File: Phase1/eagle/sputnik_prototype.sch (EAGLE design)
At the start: 6 parts, among them U1 MEGA128-M

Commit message: Added stuff to RF schematic
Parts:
- added C1, C10, C11, C12, C13, C14, C2, C3, C4, C5, C6, C7, C8, C9: (no value), rcl_custom:C-EU0603-B-NOSILK
- added L1, L2, L3, L4, L5, L6: (no value), rcl_custom:L-US0603-B-NOSILK
- added U$2: SMAJ716-ND, psas_c3_team05:SMAJ716-ND
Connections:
- new net N$10: C5.2, C7.1, L3.1
- new net N$16: C7.2, C9.2, L3.2, L5.1
- new net N$17: C11.2, C14.2, L5.2
- new net N$18: C6.2, C8.1, L4.1
- new net N$19: C10.2, C8.2, L4.2, L6.1
- new net N$20: C12.2, C13.2, L6.2
- new net N$6: C4.1, C6.1, L2.2, U$1.RFIO
- new net N$7: C2.1, C5.1, L1.2, U$1.PA_BOOST
- new net N$8: C1.2, C3.1, L1.1, L2.1, U$1.VR_PA
- new net N$9: C13.1, C14.1, U$2.CENTERCONDUCTOR
- net GND: now also C1.1, C10.1, C11.1, C12.1, C2.2, C3.2, C4.2, C9.1, U$2.OUTERCONDUCTOR

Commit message: RF schematic update. Finished PA footprint
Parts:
- added U$3: SKY65116, psas_c3_team05:SKY65116
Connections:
- net GND: now also U1.GND@2; no longer U1.GND1
- net V+: now also U1.VCC@1; no longer U1.VCC1
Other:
- note added: "William Harrington, James Heath"
- note removed: "William Harrington"
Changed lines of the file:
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@@
 <part name="U$2" library="psas_c3_team05" deviceset="SMAJ716-ND" device=""/>
 <part name="GND13" library="psas_c3_team05" deviceset="GND" device=""/>
+<part name="U$3" library="psas_c3_team05" deviceset="SKY65116" device=""/>
 </parts>
 <sheets>
 <sheet>
 <plain>
-<text x="327.66" y="30.48" size="2.54" layer="97">William Harrington</text>
+<text x="327.66" y="30.48" size="2.54" layer="97">William Harrington, James Heath</text>
 <wire x1="10.16" y1="254" x2="63.5" y2="254" width="0.1524" layer="97" style="longdash"/>
 <wire x1="63.5" y1="254" x2="63.5" y2="167.64" width="0.1524" layer="97" style="longdash"/>
@@
 <instance part="U$2" gate="G$1" x="515.62" y="345.44" rot="MR0"/>
 <instance part="GND13" gate="1" x="515.62" y="330.2"/>
+<instance part="U$3" gate="G$1" x="510.54" y="378.46"/>
 </instances>
 <busses>
@@
 <wire x1="86.36" y1="66.04" x2="68.58" y2="66.04" width="0.1524" layer="91"/>
 <junction x="68.58" y="66.04"/>
-<pinref part="U1" gate="G$1" pin="GND1"/>
+<pinref part="U1" gate="G$1" pin="GND@2"/>
 <wire x1="144.78" y1="132.08" x2="68.58" y2="132.08" width="0.1524" layer="91"/>
 <junction x="68.58" y="132.08"/>
@@
 <wire x1="144.78" y1="147.32" x2="96.52" y2="147.32" width="0.1524" layer="91"/>
 <junction x="96.52" y="147.32"/>
-<pinref part="U1" gate="G$1" pin="VCC1"/>
+<pinref part="U1" gate="G$1" pin="VCC@1"/>
 <wire x1="144.78" y1="139.7" x2="96.52" y2="139.7" width="0.1524" layer="91"/>
 <junction x="96.52" y="139.7"/>

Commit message: Added more RF schematic and made LNA footprint
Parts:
- added C15, C16, C17, C18, C19, C20, C21, C22, C23, C24, C25, C26, C27: (no value), rcl_custom:C-EU0603-B-NOSILK
- added L7, L8, L9: (no value), rcl_custom:L-US0603-B-NOSILK
- added R1: (no value), rcl_custom:R-US_0603-B-NOSILK
- added U$4: MAAL-010704, sputnik:MAAL-010704
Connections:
- new net N$21: C14.1, U$3.RFIN
- new net N$22: U$3.RFOUT
- new net N$23: C13.1
- new net N$24: L7.1, U$4.RFIN
- new net N$25: C23.2, L7.2
- new net N$26: C23.1
- new net N$27: R1.1, U$4.VBIAS
- new net N$28: U$1.RXTX
- new net N$29: U$2.CENTERCONDUCTOR
- new net N$31: L9.1
- new net N$32: C26.1, C27.1, L9.2
- net GND: now also C15.1, C16.1, C17.1, C18.1, C19.1, C20.1, C21.1, C22.1, C24.2, C25.2, C26.2, C27.2, U$3.GND, U$3.GND1, U$3.GND2, U$3.GND3, U$3.GND4, U$3.GND5, U$4.GND, U$4.GND2, U$4.NC
- net N$9: now also L8.1, U$4.RFOUT; no longer C13.1, C14.1, U$2.CENTERCONDUCTOR
- net V+: now also C15.2, C16.2, C17.2, C18.2, C19.2, C20.2, C21.2, C22.2, C24.1, C25.1, L8.2, R1.2, U$3.VCC1, U$3.VCC2, U$3.VCNT, U$3.VREF
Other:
- note added: "Switch goes here"
- moved on the sheet: C1, C10, C11, C12, C13, C14, C2, C3, C4, C5, C6, C7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

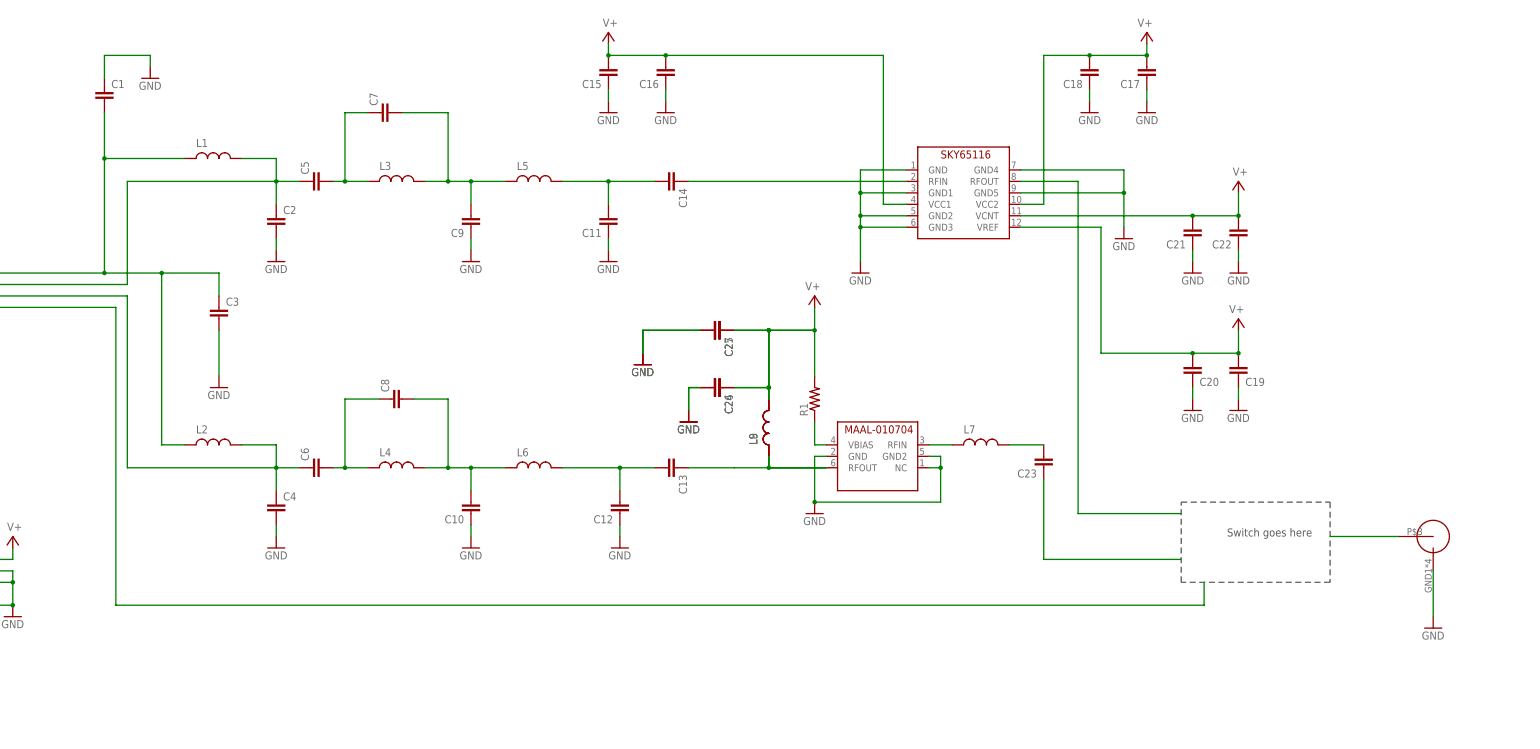
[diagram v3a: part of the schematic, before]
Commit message: Finished 1st draft RF schematic and RF switch footprint
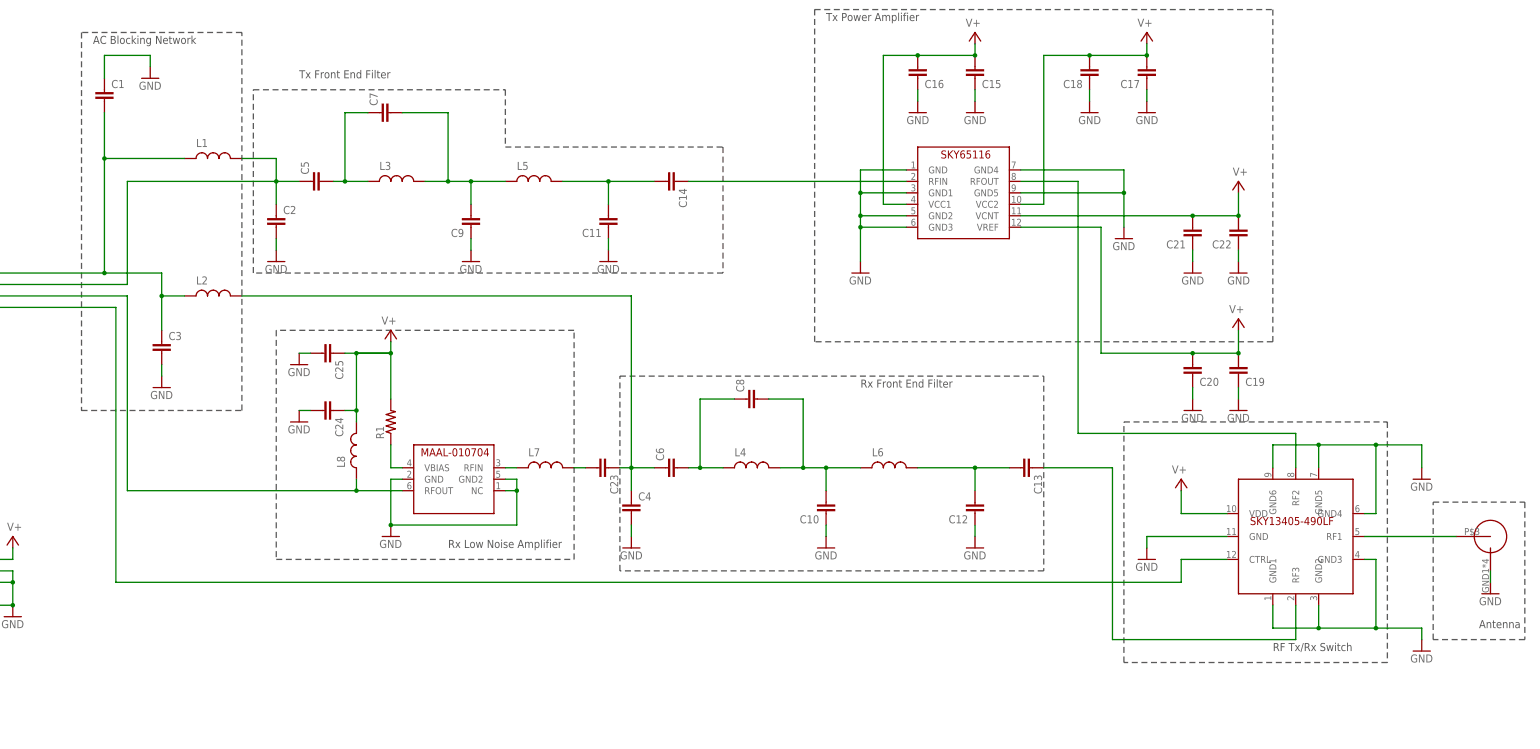
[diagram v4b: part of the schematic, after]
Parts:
- removed C26, C27: (no value), rcl_custom:C-EU0603-B-NOSILK
- removed L9: (no value), rcl_custom:L-US0603-B-NOSILK
- added U$5: SKY13405-490LF, psas_c3_team05:SKY13405-490LF
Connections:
- removed net N$23: C13.1
- removed net N$29 (its old number): U$2.CENTERCONDUCTOR
- removed net N$31: L9.1
- removed net N$32: C26.1, C27.1, L9.2
- removed net N$6: C4.1, C6.1, L2.2, U$1.RFIO
- new net N$30: U$2.CENTERCONDUCTOR, U$5.RF1
- new net N$33: C23.1, C4.1, C6.1, L2.2
- net GND: now also U$5.GND, U$5.GND1, U$5.GND2, U$5.GND3, U$5.GND4, U$5.GND5, U$5.GND6; no longer C26.2, C27.2
- net N$22: now also U$5.RF2
- net N$26: now also C13.1, U$5.RF3; no longer C23.1
- net N$28: now also U$5.CTRL
- net N$9: now also U$1.RFIO
- net V+: now also U$5.VDD
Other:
- note added: "AC Blocking Network"
- note added: "Antenna"
- note added: "RF Tx/Rx Switch"
- note added: "Rx Front End Filter"
- note added: "Rx Low Noise Amplifier"
- note added: "Tx Front End Filter"
- note added: "Tx Power Amplifier"
- note removed: "Switch goes here"
- moved on the sheet: C10, C12, C13, C15, C16, C23, C24, C25, C3, C4, C6, C8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

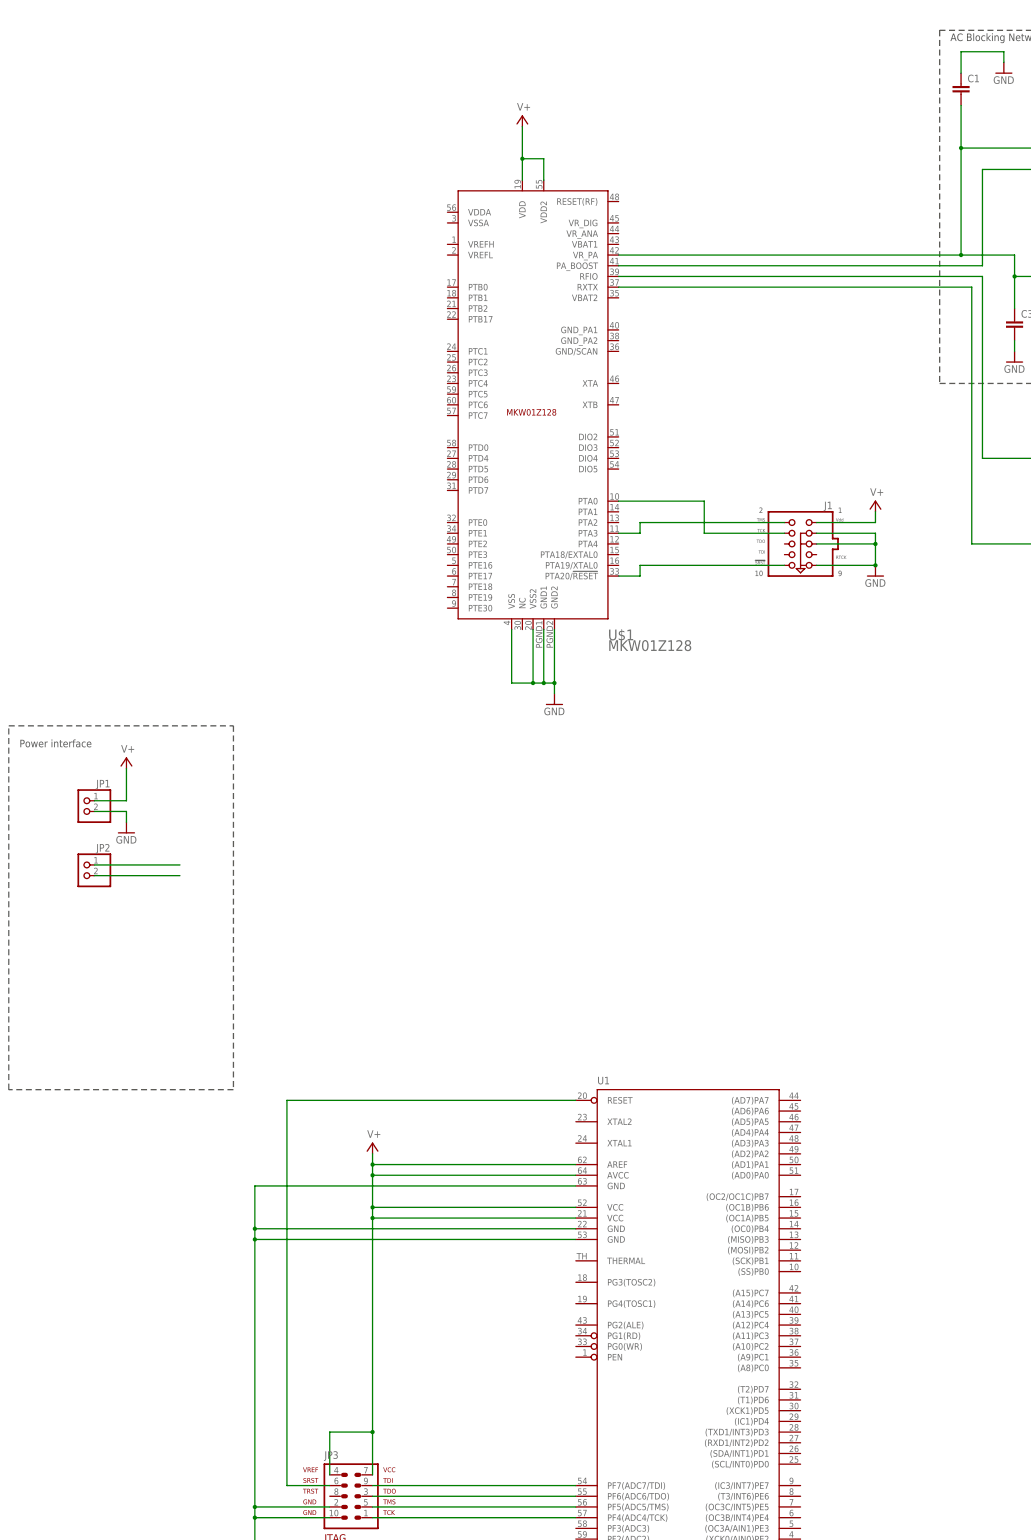
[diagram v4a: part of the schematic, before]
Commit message: Schematic checkpoint
Setup GPIO and I2C for power interface. Placed bypass caps on all power lines. Placed XTAL/Resonator. Labeled some wires.
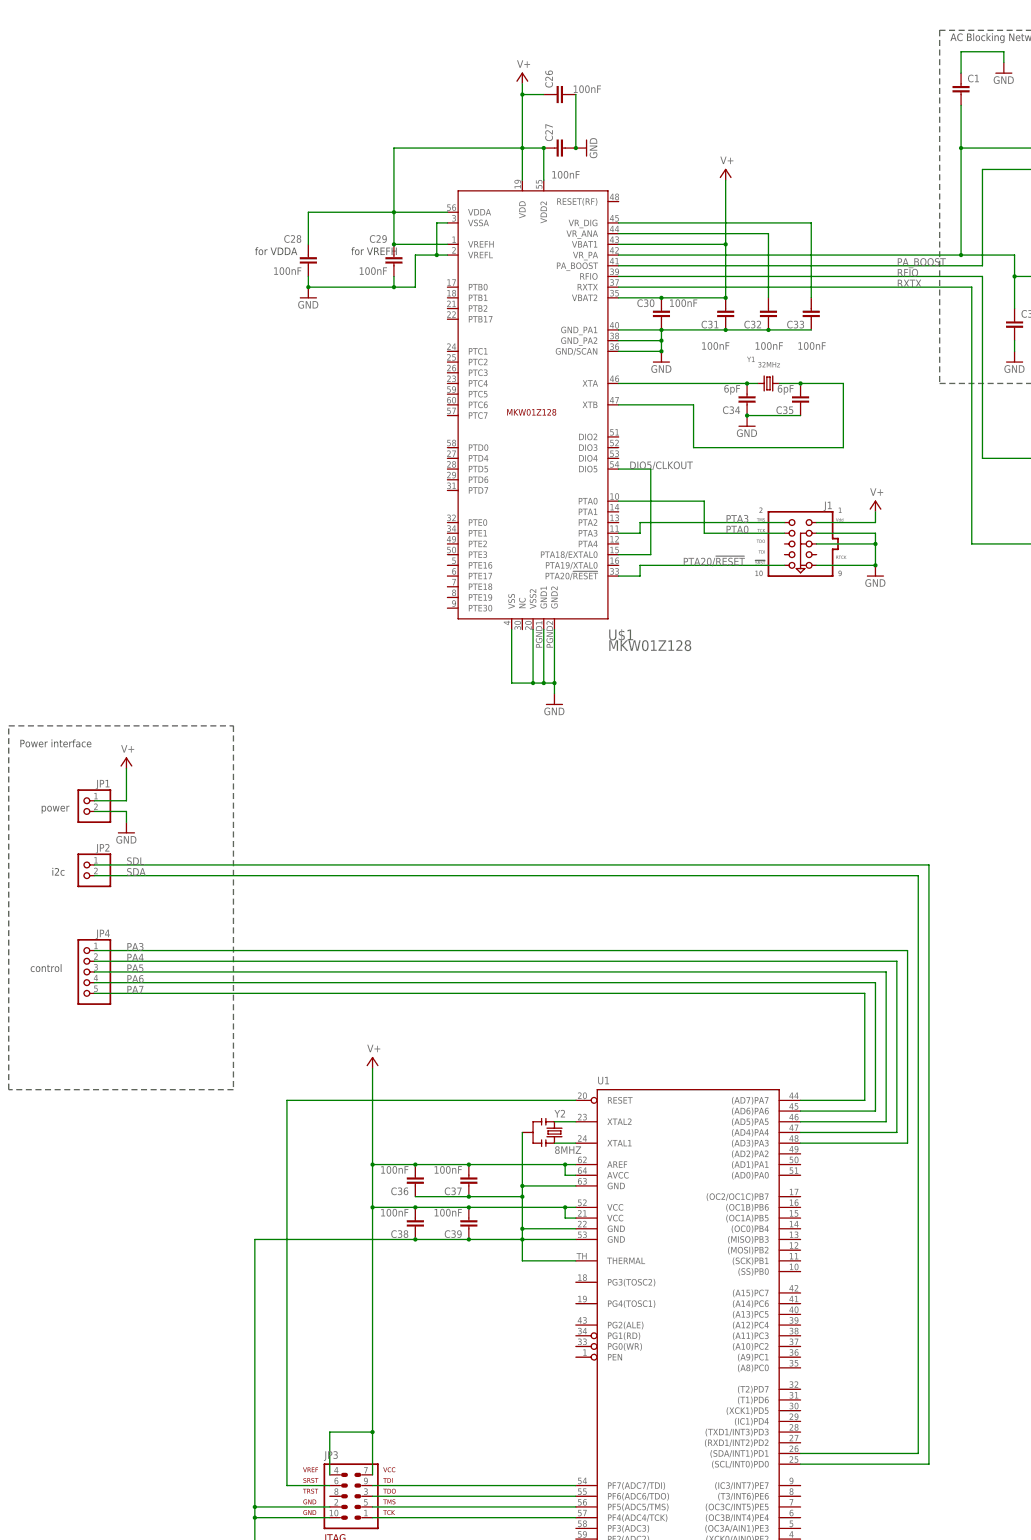
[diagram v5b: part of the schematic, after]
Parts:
- added C26, C27, C28, C29, C30, C31, C32, C33, C36, C37, C38, C39: 100nF, rcl_custom:C-EU0603-B-NOSILK
- added C34, C35: 6pF, rcl_custom:C-EU0603-B-NOSILK
- added JP4: (no value), pinhead:PINHD-1X55X2MM
- added Y1: 32MHz, microbuilder:CRYSTAL2.5X2.0MM
- added Y2: 8MHZ, Lilypad_Arduino_USB_v12:SPARKFUN-FREQCTRL_RESONATOR8MHZ
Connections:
- net N$1 renamed PTA3
- net N$2 renamed PTA0
- net N$28 renamed RXTX
- net N$5 renamed PTA20/!RESET
- net N$7 renamed PA_BOOST
- net N$9 renamed RFIO
- removed net N$3: JP2.1
- removed net N$4: JP2.2
- new net DIO5/CLKOUT: U$1.DIO5, U$1.PTA18/EXTAL0
- new net N$23: U1.XTAL2, Y2.1
- new net N$31: C32.2, U$1.VR_ANA
- new net N$34: C33.2, U$1.VR_DIG
- new net N$36: U1.XTAL1, Y2.3
- new net N$6: C34.2, U$1.XTA, Y1.1
- new net N$8: C35.2, U$1.XTB, Y1.2
- new net PA3: JP4.1, U1.(AD3)PA3
- new net PA4: JP4.2, U1.(AD4)PA4
- new net PA5: JP4.3, U1.(AD5)PA5
- new net PA6: JP4.4, U1.(AD6)PA6
- new net PA7: JP4.5, U1.(AD7)PA7
- new net SDA: JP2.2, U1.(SDA/INT1)PD1
- new net SDL: JP2.1, U1.(SCL/INT0)PD0
- net GND: now also C26.2, C27.2, C28.1, C29.1, C30.1, C31.1, C32.1, C33.1, C34.1, C35.1, C36.1, C37.1, C38.1, C39.1, U$1.GND/SCAN, U$1.GND_PA1, U$1.GND_PA2, U$1.VREFL, U$1.VSSA, U1.THERMAL, Y2.2
- net V+: now also C26.1, C27.1, C28.2, C29.2, C30.2, C31.2, C36.2, C37.2, C38.2, C39.2, U$1.VBAT1, U$1.VBAT2, U$1.VDDA, U$1.VREFH
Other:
- note added: "control"
- note added: "for VDDA"
- note added: "for VREFH"
- note added: "i2c"
- note added: "power"
